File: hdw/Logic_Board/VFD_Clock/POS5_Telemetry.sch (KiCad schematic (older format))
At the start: 15 parts

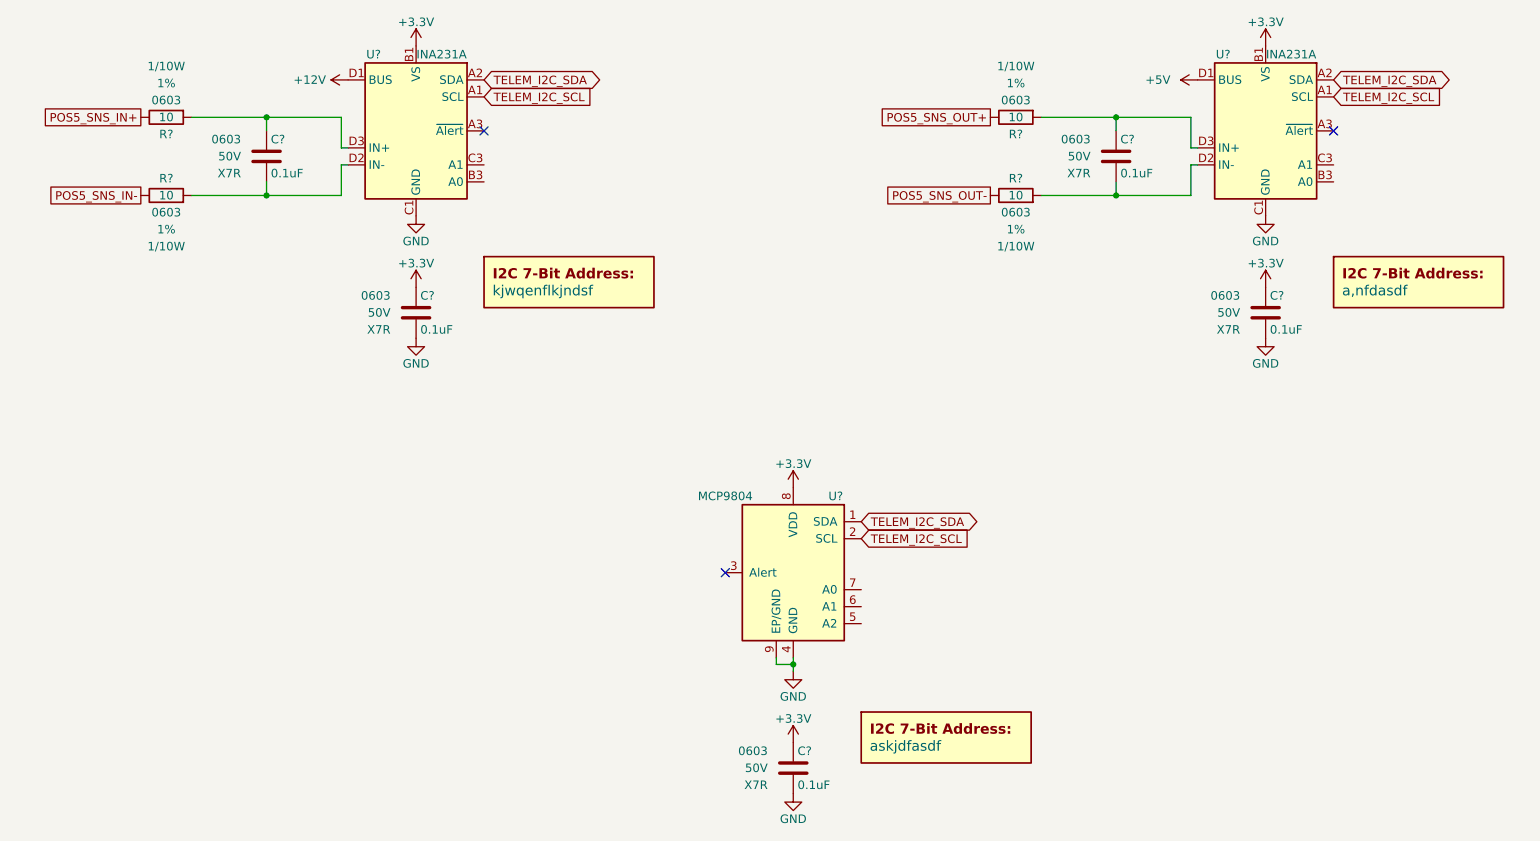
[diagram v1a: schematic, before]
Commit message: Lots of schematic additions
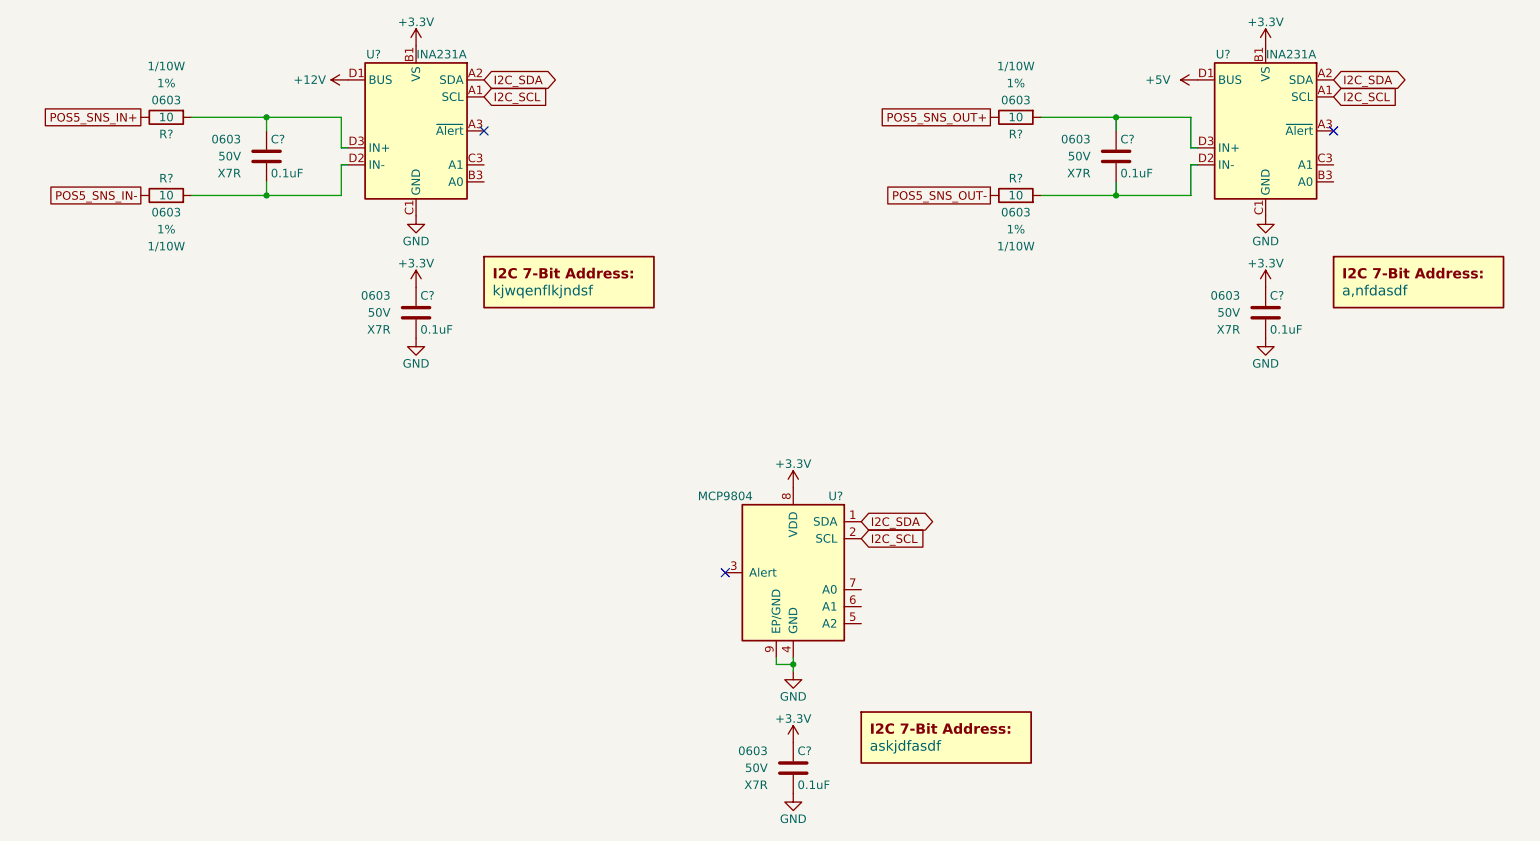
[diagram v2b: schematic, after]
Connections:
- net TELEM_I2C_SCL renamed I2C_SCL
- net TELEM_I2C_SDA renamed I2C_SDA
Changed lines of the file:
@@
 $Descr A 11000 8500
 encoding utf-8
-Sheet 22 26
+Sheet 22 28
 Title ""
 Date ""
@@
 $EndComp
 Text GLabel 3610 2040 2    50   Input ~ 0
-TELEM_I2C_SCL
+I2C_SCL
 $Comp
 L Custom_Library:C_Custom C?
@@
 $EndComp
 Text GLabel 3610 1940 2    50   BiDi ~ 0
-TELEM_I2C_SDA
+I2C_SDA
 NoConn ~ 3610 2240
 $Comp
@@
 $EndComp
 Text GLabel 5830 4640 2    50   Input ~ 0
-TELEM_I2C_SCL
+I2C_SCL
 Text GLabel 5830 4540 2    50   BiDi ~ 0
-TELEM_I2C_SDA
+I2C_SDA
 NoConn ~ 5030 4840
 $Comp
@@
 $EndComp
 Text GLabel 8610 2040 2    50   Input ~ 0
-TELEM_I2C_SCL
+I2C_SCL
 $Comp
 L Custom_Library:C_Custom C?
@@
 $EndComp
 Text GLabel 8610 1940 2    50   BiDi ~ 0
-TELEM_I2C_SDA
+I2C_SDA
 NoConn ~ 8610 2240
 $Comp

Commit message: Added backup RTC, IO connector, other stuff
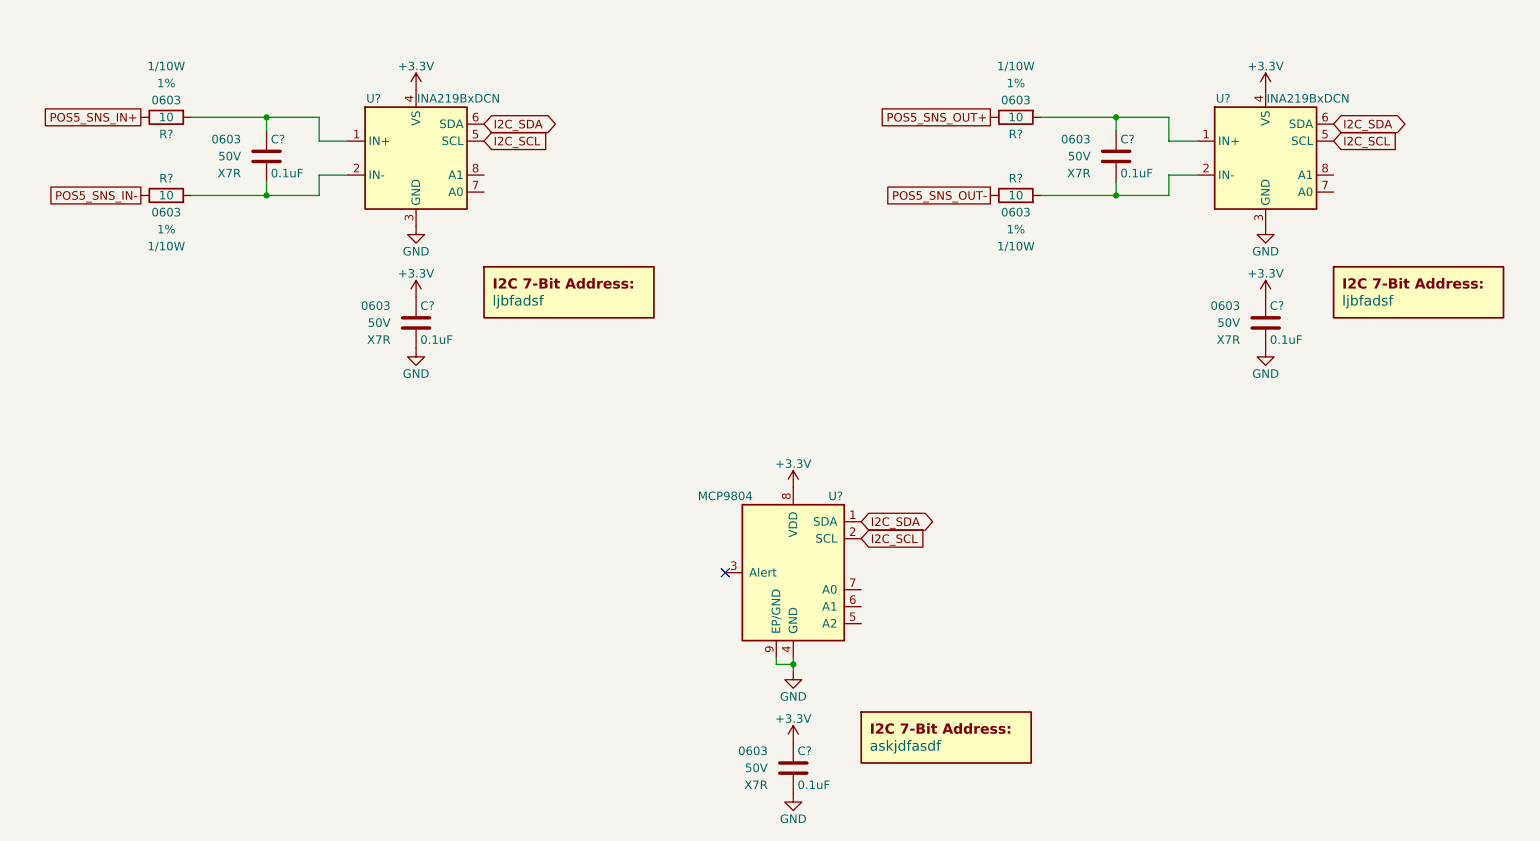
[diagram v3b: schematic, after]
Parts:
- removed C? (x4): 0.1uF, Capacitors_SMD:C_0603, symbol Custom_Library:C_Custom
- removed DOC?: a,nfdasdf, symbol Custom_Library:I2C_Address
- removed DOC?: kjwqenflkjndsf, symbol Custom_Library:I2C_Address
- removed R? (x4): 10, Resistors_SMD:R_0603, symbol Custom_Library:R_Custom
- removed U? (x2): INA231A, Custom Footprints Library:Texas_DSBGA-12_1.65x1.39mm_Layout3x4_P0.4mm, symbol Custom_Library:INA231A
- added C? (x4): 0.1uF, Capacitors_SMD:C_0603, symbol Custom_Library:C_Custom
- added DOC? (x2): ljbfadsf, symbol Custom_Library:I2C_Address
- added R? (x4): 10, Resistors_SMD:R_0603, symbol Custom_Library:R_Custom
- added U? (x2): INA219BxDCN, Package_TO_SOT_SMD:SOT-23-8, symbol Analog_ADC:INA219BxDCN
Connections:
- net +3V3: now also C?.1, C?.1, U?.4 (VS), U?.4 (VS)
- net GND: now also C?.2, C?.2, U?.3 (GND), U?.3 (GND)
- net I2C_SCL: now also U?.5 (SCL), U?.5 (SCL)
- net I2C_SDA: now also U?.6 (SDA), U?.6 (SDA)
- net POS5_SNS_IN+: now also R?.2
- net POS5_SNS_IN-: now also R?.2
- net POS5_SNS_OUT+: now also R?.2
- net POS5_SNS_OUT-: now also R?.2
- new net: C?.1, R?.1, U?.1 (IN+) (x2)
- new net: C?.2, R?.1, U?.2 (IN-) (x2)
- no-connect marks 3 -> 1

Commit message: Changed to configurable discrete gates, added VBAT stuff
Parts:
- removed C?: 0.1uF, Capacitors_SMD:C_0603, symbol Custom_Library:C_Custom
- removed DOC?: askjdfasdf, symbol Custom_Library:I2C_Address
- removed U?: MCP9804, Package_DFN_QFN:DFN-8-1EP_3x2mm_P0.5mm_EP1.3x1.5mm, symbol Sensor_Temperature:MCP9804_DFN
- added C?: 0.1uF, Capacitors_SMD:C_0603, symbol Custom_Library:C_Custom
- added DOC?: askjdfasdf, symbol Custom_Library:I2C_Address
- added U?: MCP9804, Package_DFN_QFN:DFN-8-1EP_3x2mm_P0.5mm_EP1.3x1.5mm, symbol Sensor_Temperature:MCP9804_DFN
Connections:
- net +3V3: now also C?.1, U?.8 (VDD)
- net GND: now also C?.2, U?.4 (GND), U?.9 (EP/GND)
- net I2C_SCL: now also U?.2 (SCL)
- net I2C_SDA: now also U?.1 (SDA)
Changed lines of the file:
@@
 $Comp
 L power:+3.3V #PWR?
-U 1 1 5E0BDB95
+U 1 1 5E2AA99B
 P 5430 4340
-AR Path="/5E0652BA/5E0BDB95" Ref="#PWR?"  Part="1"
-AR Path="/5E0A0E29/5E0BDB95" Ref="#PWR?"  Part="1"
-AR Path="/5E0DC084/5E0BDB95" Ref="#PWR?"  Part="1"
-AR Path="/5E0F9112/5E0BDB95" Ref="#PWR?"  Part="1"
+AR Path="/5E0652BA/5E2AA99B" Ref="#PWR?"  Part="1"
+AR Path="/5E0A0E29/5E2AA99B" Ref="#PWR?"  Part="1"
+AR Path="/5E0DC084/5E2AA99B" Ref="#PWR?"  Part="1"
+AR Path="/5E0F9112/5E2AA99B" Ref="#PWR?"  Part="1"
 F 0 "#PWR?" H 5430 4190 50  0001 C CNN
 F 1 "+3.3V" H 5430 4480 50  0000 C CNN
@@
 $Comp
 L Sensor_Temperature:MCP9804_DFN U?
-U 1 1 5E0BDB9D
+U 1 1 5E2AA99F
 P 5430 4840
-AR Path="/5B3E071A/5E0BDB9D" Ref="U?"  Part="1"
-AR Path="/5E0652BA/5E0BDB9D" Ref="U?"  Part="1"
-AR Path="/5E0A0E29/5E0BDB9D" Ref="U?"  Part="1"
-AR Path="/5E0DC084/5E0BDB9D" Ref="U?"  Part="1"
-AR Path="/5E0F9112/5E0BDB9D" Ref="U?"  Part="1"
+AR Path="/5B3E071A/5E2AA99F" Ref="U?"  Part="1"
+AR Path="/5E0652BA/5E2AA99F" Ref="U?"  Part="1"
+AR Path="/5E0A0E29/5E2AA99F" Ref="U?"  Part="1"
+AR Path="/5E0DC084/5E2AA99F" Ref="U?"  Part="1"
+AR Path="/5E0F9112/5E2AA99F" Ref="U?"  Part="1"
 F 0 "U?" H 5180 5290 50  0000 C CNN
 F 1 "MCP9804" H 5830 5290 50  0000 C CNN
@@
 $Comp
 L Custom_Library:C_Custom C?
-U 1 1 5E0CB7AA
+U 1 1 5E2AA9A4
 P 5430 5990
-AR Path="/5B3E071A/5E0CB7AA" Ref="C?"  Part="1"
-AR Path="/5E0652BA/5E0CB7AA" Ref="C?"  Part="1"
-AR Path="/5E0A0E29/5E0CB7AA" Ref="C?"  Part="1"
-AR Path="/5E0DC084/5E0CB7AA" Ref="C?"  Part="1"
-AR Path="/5E0F9112/5E0CB7AA" Ref="C?"  Part="1"
+AR Path="/5B3E071A/5E2AA9A4" Ref="C?"  Part="1"
+AR Path="/5E0652BA/5E2AA9A4" Ref="C?"  Part="1"
+AR Path="/5E0A0E29/5E2AA9A4" Ref="C?"  Part="1"
+AR Path="/5E0DC084/5E2AA9A4" Ref="C?"  Part="1"
+AR Path="/5E0F9112/5E2AA9A4" Ref="C?"  Part="1"
 F 0 "C?" H 5455 6090 50  0000 L CNN
 F 1 "0.1uF" H 5455 5890 50  0000 L CNN
@@
 $Comp
 L power:+3.3V #PWR?
-U 1 1 5E0CB7B0
+U 1 1 5E2AA9A7
 P 5430 5840
-AR Path="/5E0652BA/5E0CB7B0" Ref="#PWR?"  Part="1"
-AR Path="/5E0A0E29/5E0CB7B0" Ref="#PWR?"  Part="1"
-AR Path="/5E0DC084/5E0CB7B0" Ref="#PWR?"  Part="1"
-AR Path="/5E0F9112/5E0CB7B0" Ref="#PWR?"  Part="1"
+AR Path="/5E0652BA/5E2AA9A7" Ref="#PWR?"  Part="1"
+AR Path="/5E0A0E29/5E2AA9A7" Ref="#PWR?"  Part="1"
+AR Path="/5E0DC084/5E2AA9A7" Ref="#PWR?"  Part="1"
+AR Path="/5E0F9112/5E2AA9A7" Ref="#PWR?"  Part="1"
 F 0 "#PWR?" H 5430 5690 50  0001 C CNN
 F 1 "+3.3V" H 5430 5980 50  0000 C CNN
@@
 $Comp
 L power:GND #PWR?
-U 1 1 5E0CB7B6
+U 1 1 5E2AA9AB
 P 5430 6140
-AR Path="/5E0652BA/5E0CB7B6" Ref="#PWR?"  Part="1"
-AR Path="/5E0A0E29/5E0CB7B6" Ref="#PWR?"  Part="1"
-AR Path="/5E0DC084/5E0CB7B6" Ref="#PWR?"  Part="1"
-AR Path="/5E0F9112/5E0CB7B6" Ref="#PWR?"  Part="1"
+AR Path="/5E0652BA/5E2AA9AB" Ref="#PWR?"  Part="1"
+AR Path="/5E0A0E29/5E2AA9AB" Ref="#PWR?"  Part="1"
+AR Path="/5E0DC084/5E2AA9AB" Ref="#PWR?"  Part="1"
+AR Path="/5E0F9112/5E2AA9AB" Ref="#PWR?"  Part="1"
 F 0 "#PWR?" H 5430 5890 50  0001 C CNN
 F 1 "GND" H 5430 5990 50  0000 C CNN
@@
 $Comp
 L Custom_Library:I2C_Address DOC?
-U 1 1 5E0CB7BC
+U 1 1 5E2AA9AE
 P 6330 5860
-AR Path="/5E0652BA/5E0CB7BC" Ref="DOC?"  Part="1"
-AR Path="/5E0A0E29/5E0CB7BC" Ref="DOC?"  Part="1"
-AR Path="/5E0DC084/5E0CB7BC" Ref="DOC?"  Part="1"
-AR Path="/5E0F9112/5E0CB7BC" Ref="DOC?"  Part="1"
+AR Path="/5E0652BA/5E2AA9AE" Ref="DOC?"  Part="1"
+AR Path="/5E0A0E29/5E2AA9AE" Ref="DOC?"  Part="1"
+AR Path="/5E0DC084/5E2AA9AE" Ref="DOC?"  Part="1"
+AR Path="/5E0F9112/5E2AA9AE" Ref="DOC?"  Part="1"
 F 0 "DOC?" H 6330 6110 60  0001 C CNN
 F 1 "askjdfasdf" H 5880 5860 60  0000 L CNN
@@
 AR Path="/5E0A0E29/5E1CE364" Ref="#PWR?"  Part="1"
 AR Path="/5E052856/5E1CE364" Ref="#PWR?"  Part="1"
+AR Path="/5E0DC084/5E1CE364" Ref="#PWR?"  Part="1"
 F 0 "#PWR?" H 3210 2550 50  0001 C CNN
 F 1 "GND" H 3210 2650 50  0000 C CNN
@@
 AR Path="/5E0A0E29/5E1CE36A" Ref="#PWR?"  Part="1"
 AR Path="/5E052856/5E1CE36A" Ref="#PWR?"  Part="1"
+AR Path="/5E0DC084/5E1CE36A" Ref="#PWR?"  Part="1"
 F 0 "#PWR?" H 3210 1850 50  0001 C CNN
 F 1 "+3.3V" H 3210 2140 50  0000 C CNN
@@
 AR Path="/5E0A0E29/5E1CE375" Ref="C?"  Part="1"
 AR Path="/5E052856/5E1CE375" Ref="C?"  Part="1"
+AR Path="/5E0DC084/5E1CE375" Ref="C?"  Part="1"
 F 0 "C?" H 3235 3470 50  0000 L CNN
 F 1 "0.1uF" H 3235 3270 50  0000 L CNN
@@
 AR Path="/5E0A0E29/5E1CE37B" Ref="#PWR?"  Part="1"
 AR Path="/5E052856/5E1CE37B" Ref="#PWR?"  Part="1"
+AR Path="/5E0DC084/5E1CE37B" Ref="#PWR?"  Part="1"
 F 0 "#PWR?" H 3210 3070 50  0001 C CNN
 F 1 "+3.3V" H 3210 3360 50  0000 C CNN
@@
 AR Path="/5E0A0E29/5E1CE381" Ref="#PWR?"  Part="1"
 AR Path="/5E052856/5E1CE381" Ref="#PWR?"  Part="1"
+AR Path="/5E0DC084/5E1CE381" Ref="#PWR?"  Part="1"
 F 0 "#PWR?" H 3210 3270 50  0001 C CNN
 F 1 "GND" H 3210 3370 50  0000 C CNN
@@
 AR Path="/5E0A0E29/5E1CE388" Ref="DOC?"  Part="1"
 AR Path="/5E052856/5E1CE388" Ref="DOC?"  Part="1"
+AR Path="/5E0DC084/5E1CE388" Ref="DOC?"  Part="1"
 F 0 "DOC?" H 4110 3490 60  0001 C CNN
 F 1 "ljbfadsf" H 3660 3240 60  0000 L CNN
@@
 AR Path="/5E0A0E29/5E1CE394" Ref="C?"  Part="1"
 AR Path="/5E052856/5E1CE394" Ref="C?"  Part="1"
+AR Path="/5E0DC084/5E1CE394" Ref="C?"  Part="1"
 F 0 "C?" H 2355 2490 50  0000 L CNN
 F 1 "0.1uF" H 2355 2290 50  0000 L CNN
@@
 AR Path="/5E0A0E29/5E1CE39E" Ref="R?"  Part="1"
 AR Path="/5E052856/5E1CE39E" Ref="R?"  Part="1"
+AR Path="/5E0DC084/5E1CE39E" Ref="R?"  Part="1"
 F 0 "R?" V 1640 2620 50  0000 C CNN
 F 1 "10" V 1740 2620 50  0000 C CNN
@@
 AR Path="/5E0A0E29/5E1CE3A9" Ref="R?"  Part="1"
 AR Path="/5E052856/5E1CE3A9" Ref="R?"  Part="1"
+AR Path="/5E0DC084/5E1CE3A9" Ref="R?"  Part="1"
 F 0 "R?" V 1640 2160 50  0000 C CNN
 F 1 "10" V 1740 2160 50  0000 C CNN
@@
 AR Path="/5E0A0E29/5E1DA355" Ref="#PWR?"  Part="1"
 AR Path="/5E052856/5E1DA355" Ref="#PWR?"  Part="1"
+AR Path="/5E0DC084/5E1DA355" Ref="#PWR?"  Part="1"
 F 0 "#PWR?" H 8210 2550 50  0001 C CNN
 F 1 "GND" H 8210 2650 50  0000 C CNN
@@
 AR Path="/5E0A0E29/5E1DA35B" Ref="#PWR?"  Part="1"
 AR Path="/5E052856/5E1DA35B" Ref="#PWR?"  Part="1"
+AR Path="/5E0DC084/5E1DA35B" Ref="#PWR?"  Part="1"
 F 0 "#PWR?" H 8210 1850 50  0001 C CNN
 F 1 "+3.3V" H 8210 2140 50  0000 C CNN
@@
 AR Path="/5E0A0E29/5E1DA366" Ref="C?"  Part="1"
 AR Path="/5E052856/5E1DA366" Ref="C?"  Part="1"
+AR Path="/5E0DC084/5E1DA366" Ref="C?"  Part="1"
 F 0 "C?" H 8235 3470 50  0000 L CNN
 F 1 "0.1uF" H 8235 3270 50  0000 L CNN
@@
 AR Path="/5E0A0E29/5E1DA36C" Ref="#PWR?"  Part="1"
 AR Path="/5E052856/5E1DA36C" Ref="#PWR?"  Part="1"
+AR Path="/5E0DC084/5E1DA36C" Ref="#PWR?"  Part="1"
 F 0 "#PWR?" H 8210 3070 50  0001 C CNN
 F 1 "+3.3V" H 8210 3360 50  0000 C CNN
@@
 AR Path="/5E0A0E29/5E1DA372" Ref="#PWR?"  Part="1"
 AR Path="/5E052856/5E1DA372" Ref="#PWR?"  Part="1"
+AR Path="/5E0DC084/5E1DA372" Ref="#PWR?"  Part="1"
 F 0 "#PWR?" H 8210 3270 50  0001 C CNN
 F 1 "GND" H 8210 3370 50  0000 C CNN
@@
 AR Path="/5E0A0E29/5E1DA379" Ref="DOC?"  Part="1"
 AR Path="/5E052856/5E1DA379" Ref="DOC?"  Part="1"
+AR Path="/5E0DC084/5E1DA379" Ref="DOC?"  Part="1"
 F 0 "DOC?" H 9110 3490 60  0001 C CNN
 F 1 "ljbfadsf" H 8660 3240 60  0000 L CNN
@@
 AR Path="/5E0A0E29/5E1DA385" Ref="C?"  Part="1"
 AR Path="/5E052856/5E1DA385" Ref="C?"  Part="1"
+AR Path="/5E0DC084/5E1DA385" Ref="C?"  Part="1"
 F 0 "C?" H 7355 2490 50  0000 L CNN
 F 1 "0.1uF" H 7355 2290 50  0000 L CNN
@@
 AR Path="/5E0A0E29/5E1DA38F" Ref="R?"  Part="1"
 AR Path="/5E052856/5E1DA38F" Ref="R?"  Part="1"
+AR Path="/5E0DC084/5E1DA38F" Ref="R?"  Part="1"
 F 0 "R?" V 6640 2620 50  0000 C CNN
 F 1 "10" V 6740 2620 50  0000 C CNN
@@
 AR Path="/5E0A0E29/5E1DA39A" Ref="R?"  Part="1"
 AR Path="/5E052856/5E1DA39A" Ref="R?"  Part="1"
+AR Path="/5E0DC084/5E1DA39A" Ref="R?"  Part="1"
 F 0 "R?" V 6640 2160 50  0000 C CNN
 F 1 "10" V 6740 2160 50  0000 C CNN
